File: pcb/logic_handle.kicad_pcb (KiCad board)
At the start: 2 copper layers, 100 x 35 mm, 60 parts, among them J1 Conn_01x05_Male, Q1 BSS214NW, SW1 SW_Push, U1 NCP1117-3.3_TO252, U2 TXS0108EPW, U3 MSP430FR5739IDAR, Y1 Crystal

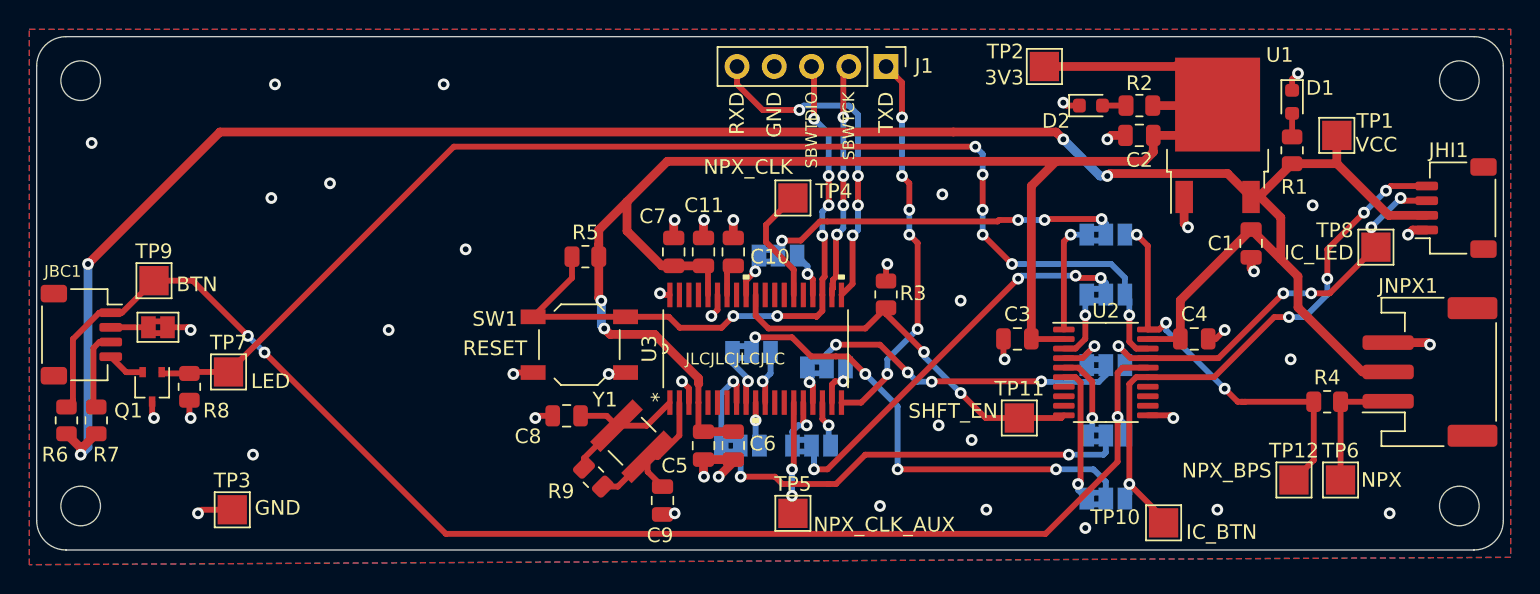
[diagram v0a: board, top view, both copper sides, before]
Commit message: pcb: implement improvements described in rev 1 bringup notes (#23)
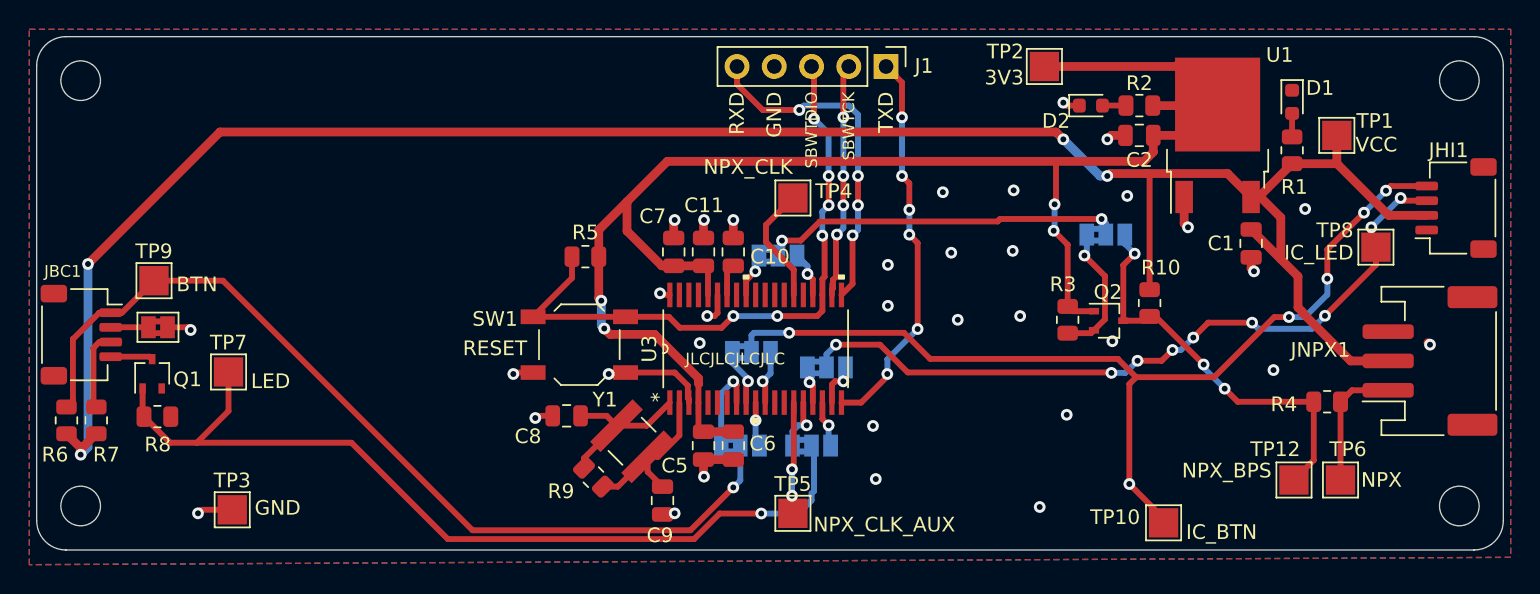
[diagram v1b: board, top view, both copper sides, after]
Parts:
- removed C3: 0.1u, Capacitor_SMD:C_0805_2012Metric
- removed C4: 10u, Capacitor_SMD:C_0805_2012Metric
- removed JP10, JP7, JP8, JP9: Jumper_3_Bridged12, Jumper:SolderJumper-3_P1.3mm_Bridged2Bar12_Pad1.0x1.5mm
- removed TP11: TestPoint, TestPoint:TestPoint_Pad_2.0x2.0mm
- removed U2: TXS0108EPW, Package_SO:TSSOP-20_4.4x6.5mm_P0.65mm
- added Q2: BSS214NW, Package_TO_SOT_SMD:SOT-323_SC-70, F.Cu at (73.1, 19.4)
- added R10: 10k, Resistor_SMD:R_0805_2012Metric, F.Cu at (75.9, 18.2)
- moved R3 12.5 mm to (70.3, 19.3), turned to 90 degrees
- moved R8 2.98 mm to (8.23, 25.9), turned to 180 degrees
- moved Q1 0.89 mm to (7.87, 23.0), turned to 90 degrees
- moved JNPX1 0.75 mm to (95.0, 22.1)
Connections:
- JP2 pad 2: LED1_MCU -> LED1
- JP3 pad 2: LED2_MCU -> IC_BTN_LED
- JP4 pad 2: BTN1_MCU -> BTN+
- JP5 pad 2: BTN2_MCU -> BTN2
- Q1 pad 2: LED- -> GND
- Q1 pad 3: GND -> LED-
- R3 pad 1: GND -> NPX_MCU_SHIFT
- R3 pad 2: SHFT_EN -> +3V3
- U3 pad 12: Net-(U3-Pad12) -> (no net)
- U3 pad 13: Net-(U3-Pad13) -> (no net)
- U3 pad 24: Net-(U3-Pad24) -> (no net)
- U3 pad 26: Net-(U3-Pad26) -> (no net)
- U3 pad 27: Net-(U3-Pad27) -> (no net)
- U3 pad 28: Net-(U3-Pad28) -> (no net)
- U3 pad 29: SHFT_EN -> (no net)
- U3 pad 31: Net-(U3-Pad31) -> (no net)
- U3 pad 35: Net-(U3-Pad35) -> (no net)
- U3 pad 36: Net-(U3-Pad36) -> (no net)
- U3 pad 37: Net-(U3-Pad37) -> (no net)
- U3 pad 5: Net-(U3-Pad5) -> (no net)
- U3 pad 6: Net-(U3-Pad6) -> (no net)
- U3 pad 7: Net-(U3-Pad7) -> (no net)
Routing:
- net BTN+: track 96.6 -> 62.8 mm, vias 3 -> 1
- net BTN2_MCU: track 32.8 -> 0.00 mm, vias 4 -> 0
- net BTN1_MCU: track 29.3 -> 0.00 mm, vias 2 -> 0
- net LED1_MCU: track 28.1 -> 0.00 mm, vias 4 -> 0
- net BTN2: track 39.2 -> 67.2 mm, vias 5 -> 6
- net SHFT_EN: track 27.0 -> 0.00 mm, vias 2 -> 0
- net LED1: track 85.1 -> 61.6 mm, vias 6 -> 1
- net LED2_MCU: track 22.2 -> 0.00 mm, vias 4 -> 0
- net IC_BTN_LED: track 28.7 -> 50.2 mm, vias 5 -> 9
- net GND: track 40.9 -> 30.4 mm, vias 46 -> 34
- net BTN2_MCU_SHIFT: track 9.54 -> 0.00 mm, vias 1 -> 0
- net BTN1_MCU_SHIFT: track 6.17 -> 0.00 mm, vias 1 -> 0
- net LED1_MCU_SHIFT: track 4.79 -> 0.00 mm, vias 1 -> 0
- net VCC: track 150.0 -> 146.0 mm
- net LED2_MCU_SHIFT: track 3.94 -> 0.00 mm, vias 1 -> 0
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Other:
- board text added: "LitePog Logic Board Rev 2"
- board text removed: "LitePog Logic Board Rev 1"
- board text removed: "SHFT_EN"

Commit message: Revert "pcb: implement improvements described in rev 1 bringup notes (#23)"
This reverts commit 01e55846632a9cef383a24172751afed95ee1909.
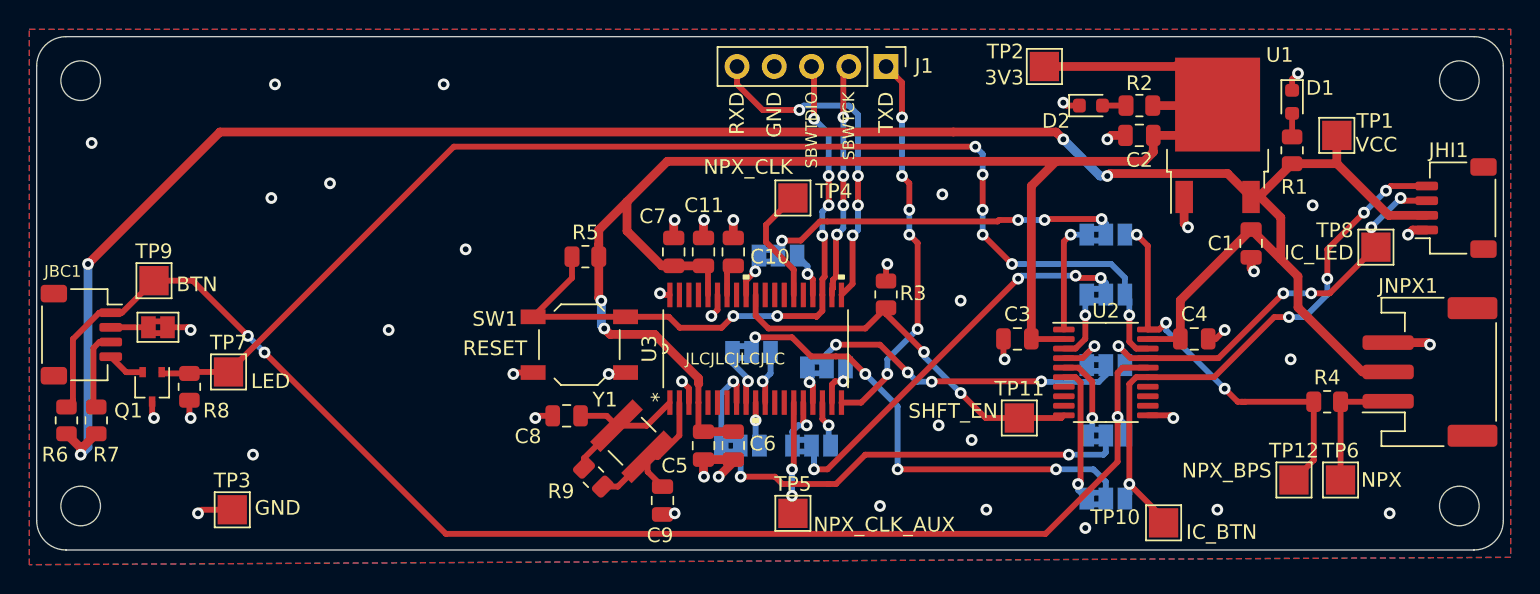
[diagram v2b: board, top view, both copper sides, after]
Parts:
- removed Q2: BSS214NW, Package_TO_SOT_SMD:SOT-323_SC-70
- removed R10: 10k, Resistor_SMD:R_0805_2012Metric
- added C3: 0.1u, Capacitor_SMD:C_0805_2012Metric, F.Cu at (66.9, 20.6)
- added C4: 10u, Capacitor_SMD:C_0805_2012Metric, F.Cu at (78.9, 20.6)
- added JP10: Jumper_3_Bridged12, Jumper:SolderJumper-3_P1.3mm_Bridged2Bar12_Pad1.0x1.5mm, B.Cu at (72.9, 31.5)
- added JP7: Jumper_3_Bridged12, Jumper:SolderJumper-3_P1.3mm_Bridged2Bar12_Pad1.0x1.5mm, B.Cu at (72.9, 17.6)
- added JP8: Jumper_3_Bridged12, Jumper:SolderJumper-3_P1.3mm_Bridged2Bar12_Pad1.0x1.5mm, B.Cu at (72.9, 22.4)
- added JP9: Jumper_3_Bridged12, Jumper:SolderJumper-3_P1.3mm_Bridged2Bar12_Pad1.0x1.5mm, B.Cu at (72.9, 27.2)
- added TP11: TestPoint, TestPoint:TestPoint_Pad_2.0x2.0mm, F.Cu at (67.0, 26.0)
- added U2: TXS0108EPW, Package_SO:TSSOP-20_4.4x6.5mm_P0.65mm, F.Cu at (72.9, 22.9)
- moved R3 12.5 mm to (57.9, 17.6), turned to 270 degrees
- moved R8 2.98 mm to (10.4, 23.9), turned to 90 degrees
- moved Q1 0.89 mm to (7.87, 23.9), turned to 270 degrees
- moved JNPX1 0.75 mm to (95.0, 22.9)
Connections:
- JP2 pad 2: LED1 -> LED1_MCU
- JP3 pad 2: IC_BTN_LED -> LED2_MCU
- JP4 pad 2: BTN+ -> BTN1_MCU
- JP5 pad 2: BTN2 -> BTN2_MCU
- Q1 pad 2: GND -> LED-
- Q1 pad 3: LED- -> GND
- R3 pad 1: NPX_MCU_SHIFT -> GND
- R3 pad 2: +3V3 -> SHFT_EN
- U3 pad 12: (no net) -> Net-(U3-Pad12)
- U3 pad 13: (no net) -> Net-(U3-Pad13)
- U3 pad 24: (no net) -> Net-(U3-Pad24)
- U3 pad 26: (no net) -> Net-(U3-Pad26)
- U3 pad 27: (no net) -> Net-(U3-Pad27)
- U3 pad 28: (no net) -> Net-(U3-Pad28)
- U3 pad 29: (no net) -> SHFT_EN
- U3 pad 31: (no net) -> Net-(U3-Pad31)
- U3 pad 35: (no net) -> Net-(U3-Pad35)
- U3 pad 36: (no net) -> Net-(U3-Pad36)
- U3 pad 37: (no net) -> Net-(U3-Pad37)
- U3 pad 5: (no net) -> Net-(U3-Pad5)
- U3 pad 6: (no net) -> Net-(U3-Pad6)
- U3 pad 7: (no net) -> Net-(U3-Pad7)
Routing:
- net BTN+: track 62.8 -> 96.6 mm, vias 1 -> 3
- net BTN2_MCU: track 0.00 -> 32.8 mm, vias 0 -> 4
- net BTN1_MCU: track 0.00 -> 29.3 mm, vias 0 -> 2
- net LED1_MCU: track 0.00 -> 28.1 mm, vias 0 -> 4
- net BTN2: track 67.2 -> 39.2 mm, vias 6 -> 5
- net SHFT_EN: track 0.00 -> 27.0 mm, vias 0 -> 2
- net LED1: track 61.6 -> 85.1 mm, vias 1 -> 6
- net LED2_MCU: track 0.00 -> 22.2 mm, vias 0 -> 4
- net IC_BTN_LED: track 50.2 -> 28.7 mm, vias 9 -> 5
- net GND: track 30.4 -> 40.9 mm, vias 34 -> 46
- net BTN2_MCU_SHIFT: track 0.00 -> 9.54 mm, vias 0 -> 1
- net BTN1_MCU_SHIFT: track 0.00 -> 6.17 mm, vias 0 -> 1
- net LED1_MCU_SHIFT: track 0.00 -> 4.79 mm, vias 0 -> 1
- net VCC: track 146.0 -> 150.0 mm
- net LED2_MCU_SHIFT: track 0.00 -> 3.94 mm, vias 0 -> 1
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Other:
- board text added: "LitePog Logic Board Rev 1"
- board text added: "SHFT_EN"
- board text removed: "LitePog Logic Board Rev 2"
